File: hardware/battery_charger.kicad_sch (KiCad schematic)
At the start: 14 parts, among them Q3 FDMC8327L, Q4 FDMC8327L, U3 LTC4162IUFD-FFSM_PBF

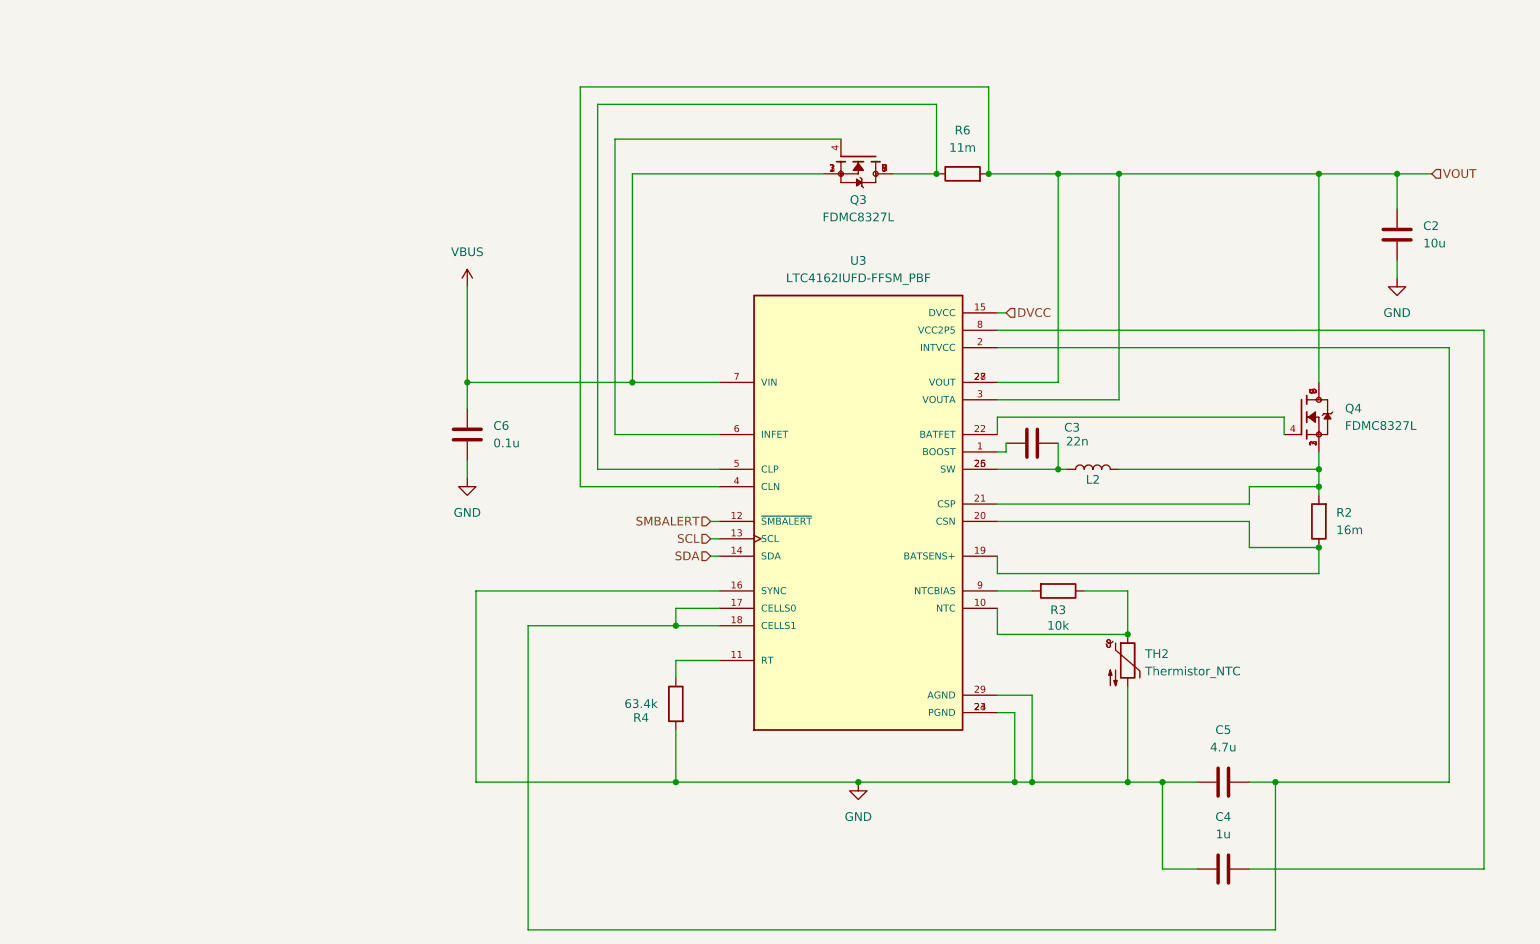
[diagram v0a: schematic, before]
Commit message: add correct battery charger schematic
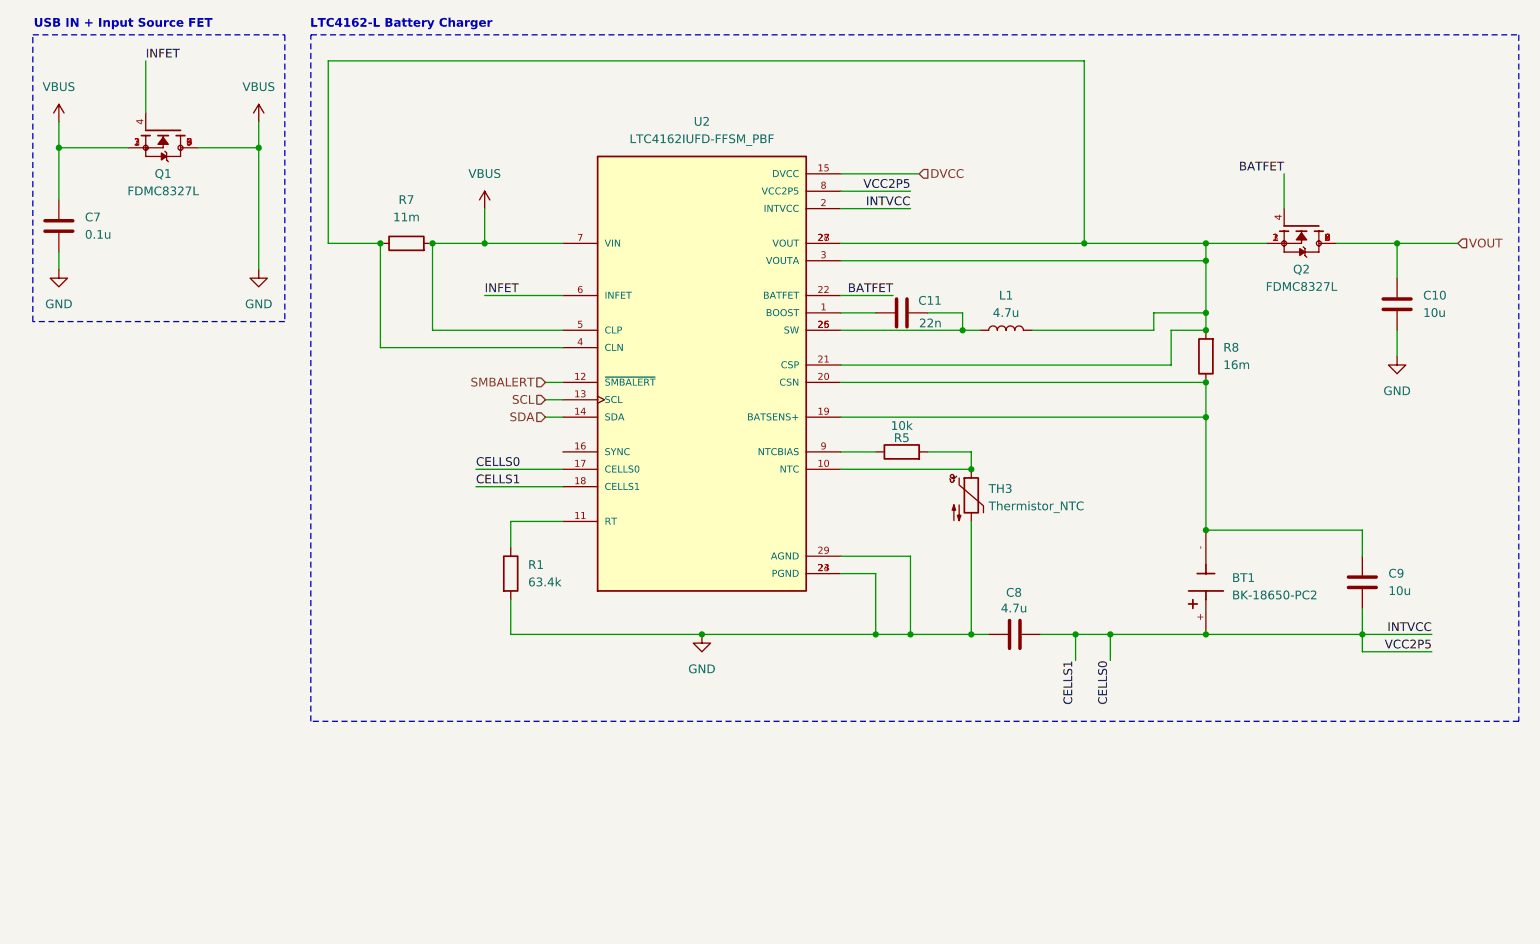
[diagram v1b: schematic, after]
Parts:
- removed C2: 10u, symbol Device:C
- removed C3: 22n, symbol Device:C
- removed C4: 1u, symbol Device:C
- removed C5: 4.7u, symbol Device:C
- removed C6: 0.1u, symbol Device:C
- removed L2: 4.7u, symbol Device:L
- removed Q3, Q4: FDMC8327L, FDMC8327L:TRANS_FDMC8327L, symbol FDMC8327L:FDMC8327L
- removed R2: 16m, symbol Device:R
- removed R3: 10k, symbol Device:R
- removed R4: 63.4k, symbol Device:R
- removed R6: 11m, symbol Device:R
- removed TH2: Thermistor_NTC, symbol Device:Thermistor_NTC
- removed U3: LTC4162IUFD-FFSM_PBF, LTC4162IUFD-FFSM_PBF:QFN50P500X400X80-29N, symbol LTC4162IUFD-FFSM_PBF:LTC4162IUFD-FFSM_PBF
- added BT1: BK-18650-PC2, BK-18650-PC2:BAT_BK-18650-PC2, symbol BK-18650-PC2:BK-18650-PC2
- added C10, C9: 10u, symbol Device:C
- added C11: 22n, symbol Device:C
- added C7: 0.1u, symbol Device:C
- added C8: 4.7u, symbol Device:C
- added L1: 4.7u, symbol Device:L
- added Q1, Q2: FDMC8327L, FDMC8327L:TRANS_FDMC8327L, symbol FDMC8327L:FDMC8327L
- added R1: 63.4k, symbol Device:R
- added R5: 10k, symbol Device:R
- added R7: 11m, symbol Device:R
- added R8: 16m, symbol Device:R
- added TH3: Thermistor_NTC, symbol Device:Thermistor_NTC
- added U2: LTC4162IUFD-FFSM_PBF, LTC4162IUFD-FFSM_PBF:QFN50P500X400X80-29N, symbol LTC4162IUFD-FFSM_PBF:LTC4162IUFD-FFSM_PBF
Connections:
- net DVCC: now also U2.15 (DVCC)
- net GND: now also C10.2, C7.1, C7.2, C8.2, Q1.1, Q1.2, Q1.3, Q1.5, Q1.6, Q1.7, Q1.8, Q1.9, R1.2, R7.2, TH3.2, U2.23 (PGND), U2.24 (PGND), U2.29 (AGND), U2.5 (CLP), U2.7 (VIN)
- net SCL: now also U2.13 (SCL)
- net SDA: now also U2.14 (SDA)
- net SMBALERT: now also U2.12 (~{SMBALERT})
- net VOUT: now also C10.1, Q2.5, Q2.6, Q2.7, Q2.8, Q2.9
- new net: BT1.-, C9.1, R8.1, U2.19 (BATSENS+), U2.20 (CSN)
- new net: L1.2, Q2.1, Q2.2, Q2.3, R7.1, R8.2, U2.21 (CSP), U2.27 (VOUT), U2.28 (VOUT), U2.3 (VOUTA), U2.4 (CLN)
- new net: R1.1, U2.11 (RT)
- new net: C11.1, U2.1 (BOOST)
- new net: R5.2, TH3.1, U2.10 (NTC)
- new net: C11.2, L1.1, U2.25 (SW), U2.26 (SW)
- new net: R5.1, U2.9 (NTCBIAS)
- new net BATFET: Q2.4, U2.22 (BATFET)
- new net CELLS0: BT1.+, C8.1, C9.2, U2.17 (CELLS0), U2.18 (CELLS1), U2.2 (INTVCC), U2.8 (VCC2P5)
- new net INFET: Q1.4, U2.6 (INFET)
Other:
- note added: "LTC4162-L Battery Charger"
- note added: "USB IN + Input Source FET"

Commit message: implement cell modem
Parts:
- added D2: LED, symbol Device:LED
- added R15: 10k, symbol Device:R
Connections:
- net GND: now also D2.1 (K)
- net VOUT: now also R15.2
- new net: D2.2 (A), R15.1

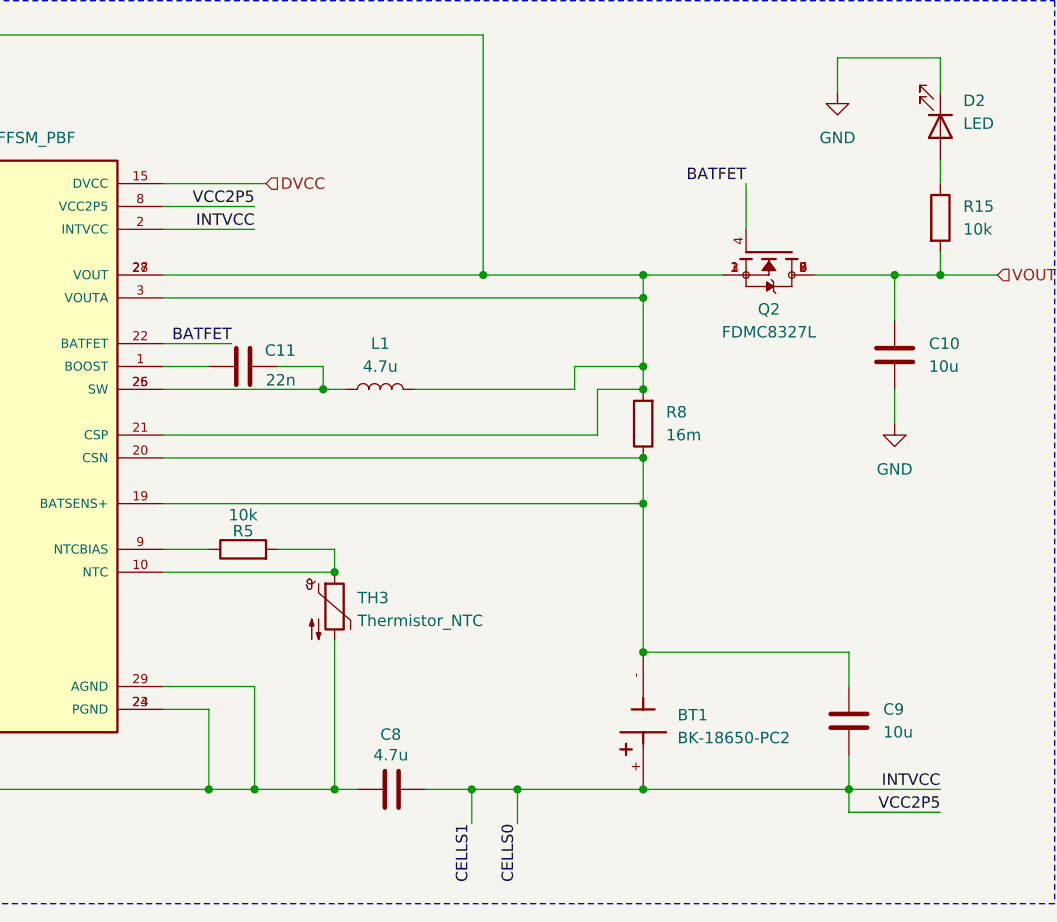
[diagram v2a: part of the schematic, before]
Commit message: begin stm32 implementation and remove battery charger for simplicity
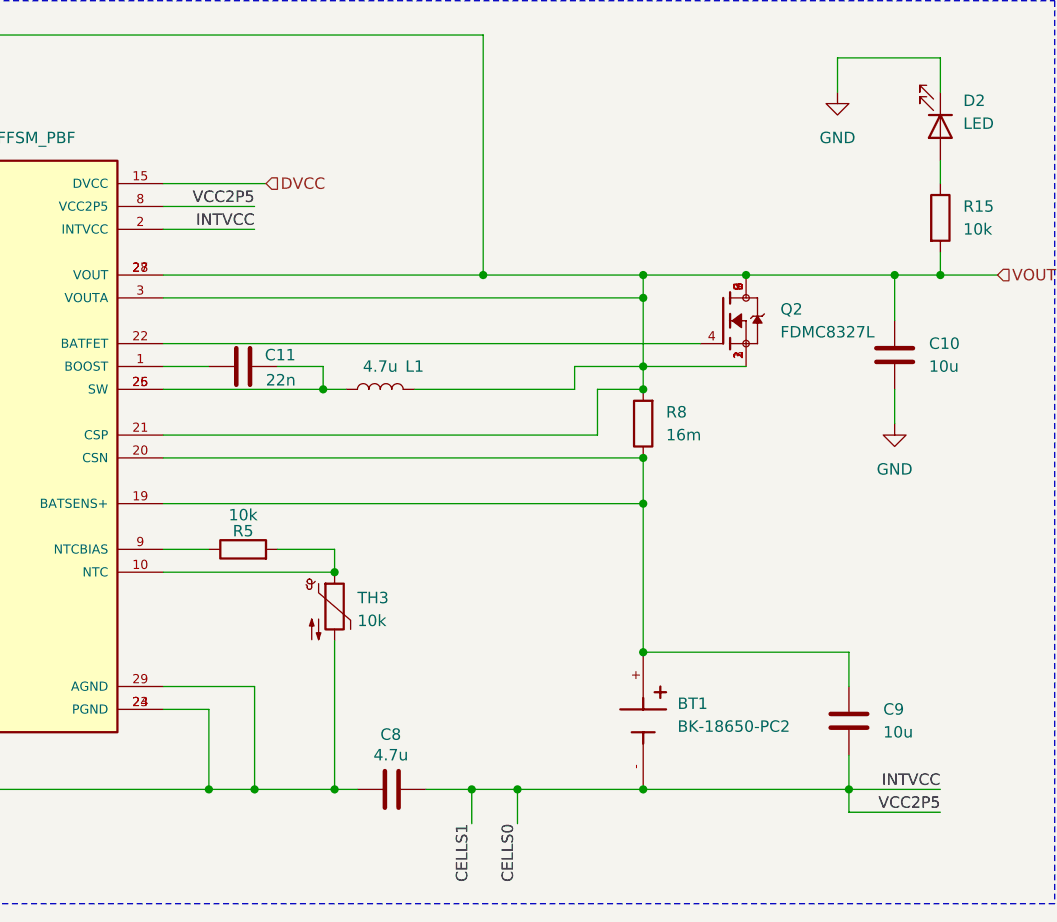
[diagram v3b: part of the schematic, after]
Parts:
- TH3: value Thermistor_NTC -> 10k
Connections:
- net CELLS0: now also BT1.-; no longer BT1.+
- net VOUT: now also L1.2, Q2.1, Q2.2, Q2.3, R7.1, R8.2, U2.21 (CSP), U2.27 (VOUT), U2.28 (VOUT), U2.3 (VOUTA), U2.4 (CLN)
- net at C9.1, R8.1, U2.19 (BATSENS+)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: now also BT1.+; no longer BT1.-
- net BATFET: no longer names the net of Q2.4, U2.22 (BATFET)
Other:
- moved on the sheet: BT1, Q2
